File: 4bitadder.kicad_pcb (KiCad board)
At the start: 2 copper layers, 100 x 110 mm, 29 parts, among them SW1 1A, SW10 MASTER_SW, SW11 VOLTS_SW, SW2 2A, SW3 4A, SW4 8A, SW5 1B, SW6 2B, SW7 4B, SW8 8B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

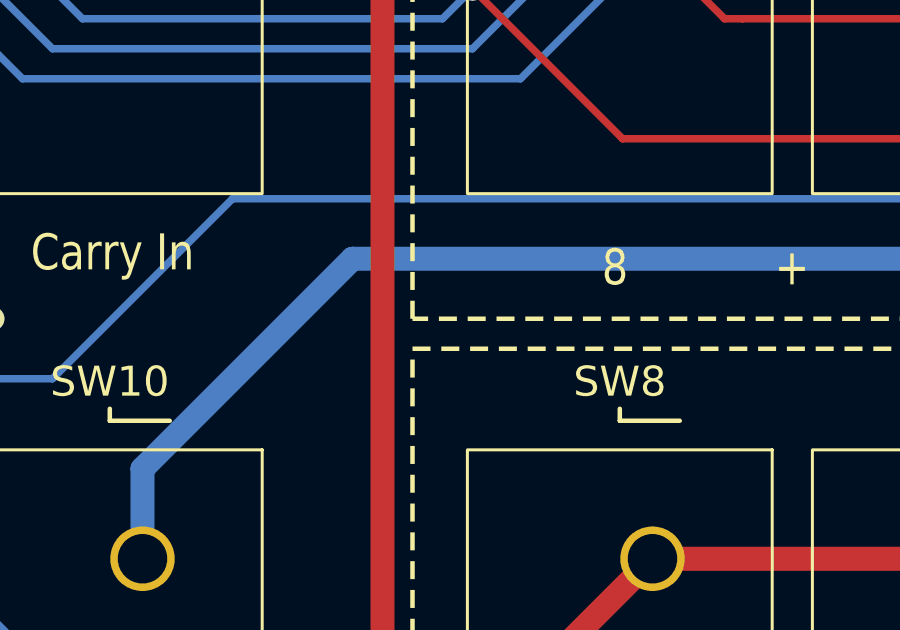
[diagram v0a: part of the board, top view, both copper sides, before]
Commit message: Change PCB Colour.
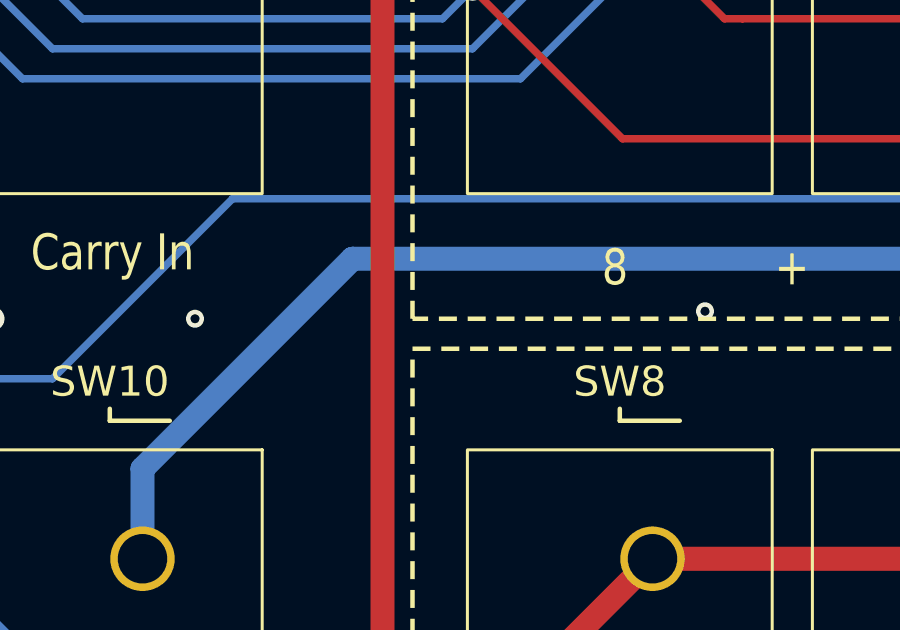
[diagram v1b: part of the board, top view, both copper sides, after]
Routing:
- net -BATT: vias 13 -> 15
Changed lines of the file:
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@@
   (via (at 85 72) (size 0.8) (drill 0.4) (layers "F.Cu" "B.Cu") (free) (net 2))
   (via (at 118 75) (size 1) (drill 0.4) (layers "F.Cu" "B.Cu") (net 2))
+  (via (at 80.75 116.75) (size 0.6) (drill 0.3) (layers "F.Cu" "B.Cu") (free) (net 2))
   (via (at 57 117) (size 0.8) (drill 0.4) (layers "F.Cu" "B.Cu") (free) (net 2))
   (via (at 73.3995 84) (size 1) (drill 0.4) (layers "F.Cu" "B.Cu") (net 2))
   (via (at 117 117) (size 0.8) (drill 0.4) (layers "F.Cu" "B.Cu") (free) (net 2))
   (via (at 70 83) (size 0.8) (drill 0.4) (layers "F.Cu" "B.Cu") (free) (net 2))
+  (via (at 63.75 117) (size 0.6) (drill 0.3) (layers "F.Cu" "B.Cu") (free) (net 2))
   (via (at 76 91) (size 0.8) (drill 0.4) (layers "F.Cu" "B.Cu") (free) (net 2))
   (segment (start 59 75) (end 58 75) (width 0.8) (layer "B.Cu") (net 2))

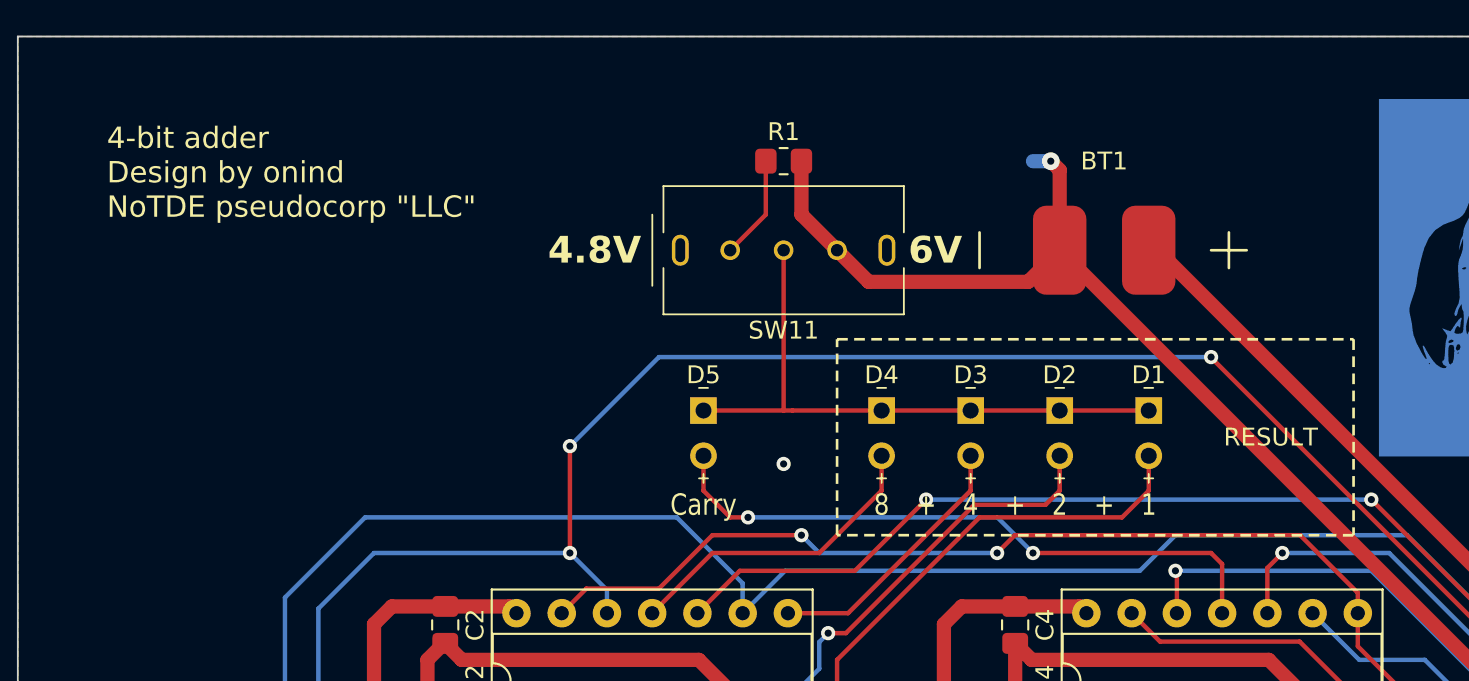
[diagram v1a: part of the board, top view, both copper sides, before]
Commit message: Repair footprint library. idk what happened there.
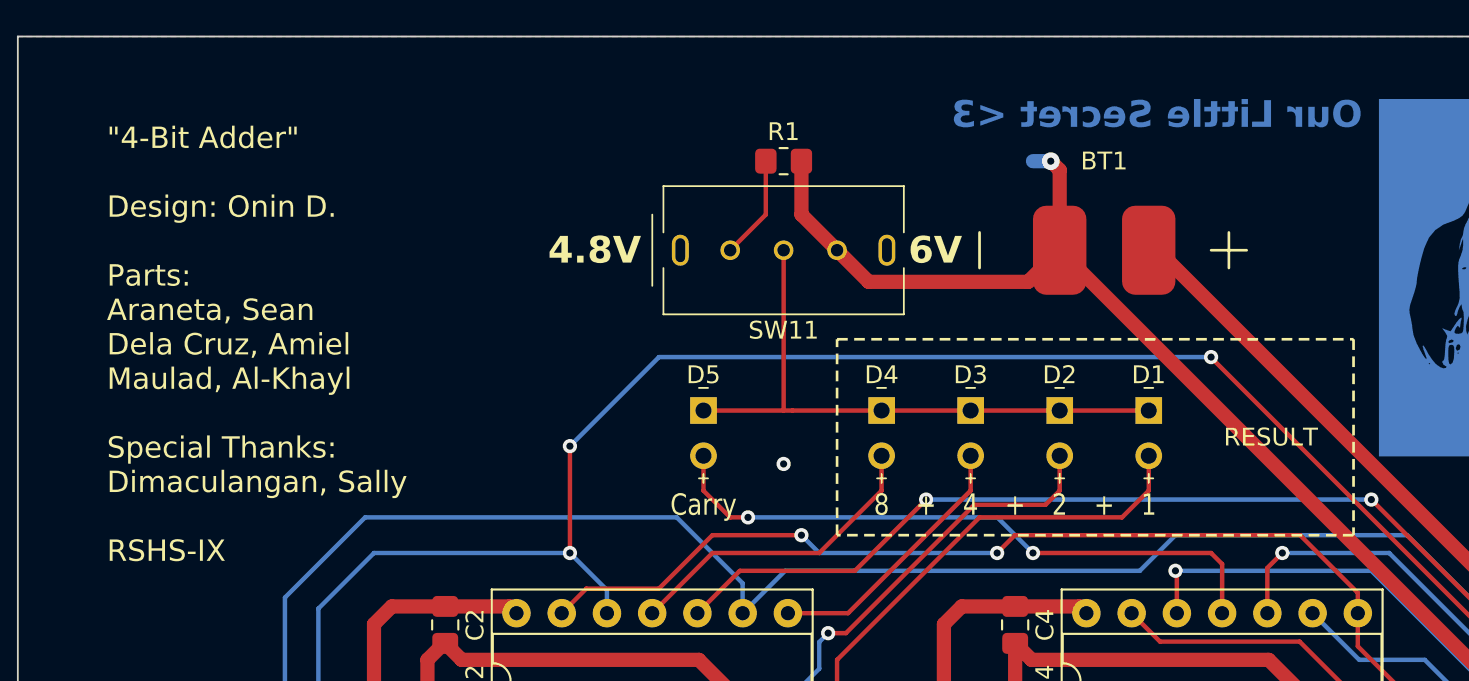
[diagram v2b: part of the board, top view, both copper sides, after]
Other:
- board text added: "Our Little Secret <3"
- board text added: "{dblquote}4-Bit Adder{dblquote} Design: Onin D. Parts: Araneta, Sean Dela Cruz, Amiel Maulad, Al-Khayl Special Thanks: Dimaculangan, Sally RSHS-IX"
- board text removed: "4-bit adder Design by onind NoTDE pseudocorp {dblquote}LLC{dblquote}"
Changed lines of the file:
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@@
   (gr_rect (start 36 34) (end 136 144)
     (stroke (width 0.1) (type default)) (fill none) (layer "Edge.Cuts"))
+  (gr_text "Our Little Secret <3" (at 111.5 37.5) (layer "B.Cu" knockout)
+    (effects (font (size 1.5 1.5) (thickness 0.3) bold) (justify left top mirror))
+  )
   (gr_text "JLCJLCJLCJLC" (at 41 42) (layer "B.SilkS")
     (effects (font (size 1 1) (thickness 0.15)) (justify right bottom mirror))
@@
     (effects (font (size 1 1) (thickness 0.15)) (justify right bottom mirror))
   )
-  (gr_text "4-bit adder\nDesign by onind\nNoTDE pseudocorp {dblquote}LLC{dblquote}" (at 41 39) (layer "F.SilkS")
+  (gr_text "{dblquote}4-Bit Adder{dblquote}\n\nDesign: Onin D.\n\nParts:\nAraneta, Sean\nDela Cruz, Amiel\nMaulad, Al-Khayl\n\nSpecial Thanks:\nDimaculangan, Sally\n\nRSHS-IX" (at 41 39) (layer "F.SilkS")
     (effects (font (size 1.2 1.2) (thickness 0.15)) (justify left top))
   )

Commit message: Finalise credits.
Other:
- board text added: "{dblquote}4-Bit Adder{dblquote} Design: Onin D. Components: Araneta, Sean Dela Cruz, Amiel Maulad, Al-Khayl Special Thanks: Dimaculangan, Sally RSHS-IX"
- board text removed: "{dblquote}4-Bit Adder{dblquote} Design: Onin D. Parts: Araneta, Sean Dela Cruz, Amiel Maulad, Al-Khayl Special Thanks: Dimaculangan, Sally RSHS-IX"
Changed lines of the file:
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@@
     (effects (font (size 1 1) (thickness 0.15)) (justify right bottom mirror))
   )
-  (gr_text "{dblquote}4-Bit Adder{dblquote}\n\nDesign: Onin D.\n\nParts:\nAraneta, Sean\nDela Cruz, Amiel\nMaulad, Al-Khayl\n\nSpecial Thanks:\nDimaculangan, Sally\n\nRSHS-IX" (at 41 39) (layer "F.SilkS")
+  (gr_text "{dblquote}4-Bit Adder{dblquote}\n\nDesign: Onin D.\n\nComponents:\nAraneta, Sean\nDela Cruz, Amiel\nMaulad, Al-Khayl\n\nSpecial Thanks:\nDimaculangan, Sally\n\nRSHS-IX" (at 41 39) (layer "F.SilkS")
     (effects (font (size 1.2 1.2) (thickness 0.15)) (justify left top))
   )

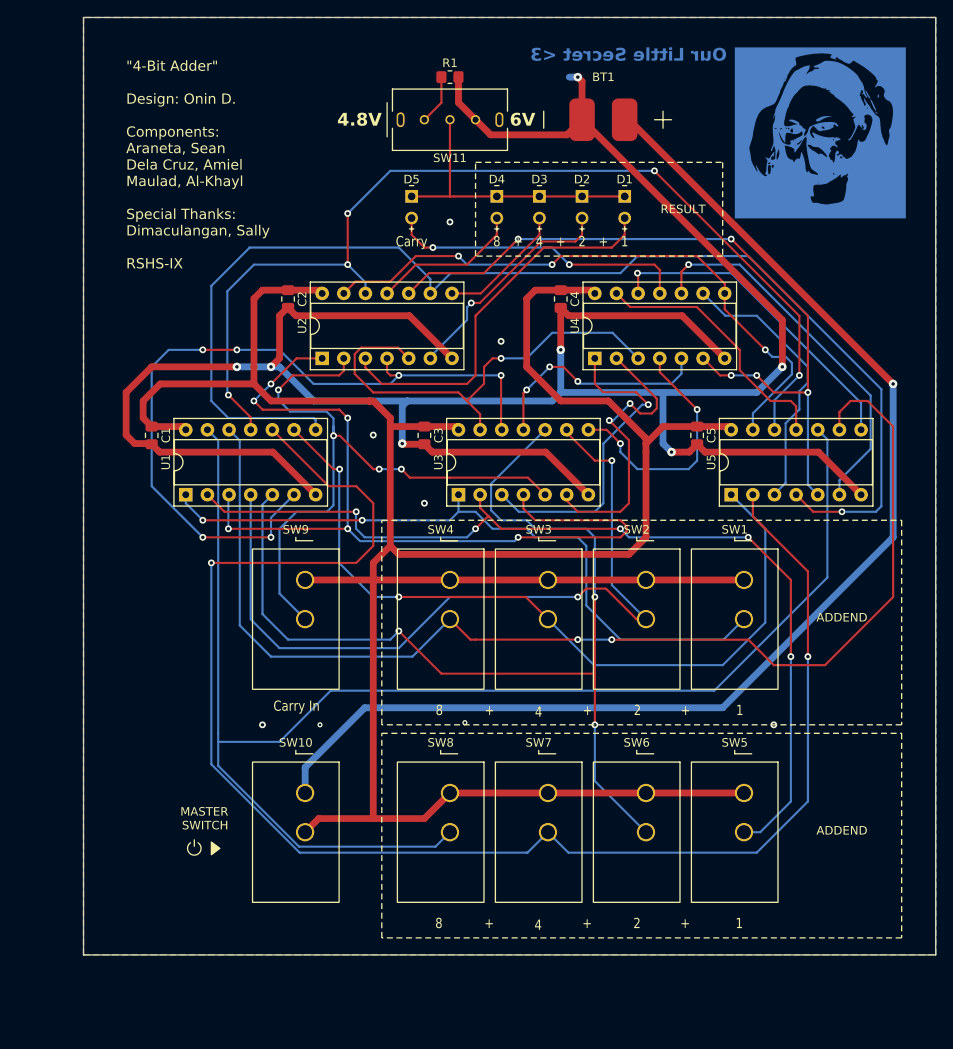
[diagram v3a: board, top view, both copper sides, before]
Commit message: Change switch design. Unroute all vias.
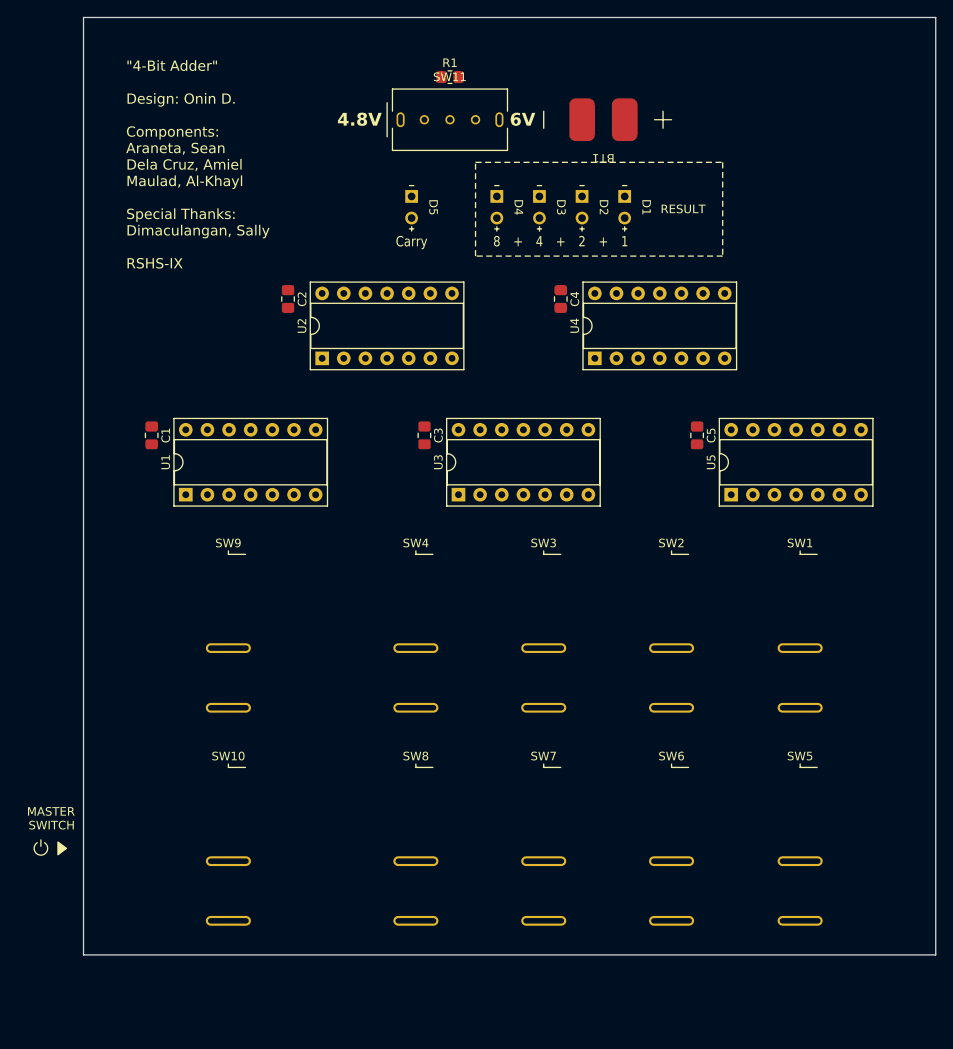
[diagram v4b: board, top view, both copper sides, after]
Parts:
- removed G***: NICA, _4bitadder:NicaPortrait
- BT1: footprint _4bitadder:PAD_Battery Terminal -> 4bitadder:PAD_Battery Terminal
- D1, D2, D3, D4, D5: footprint _4bitadder:LED_WP710A10SURDK5V -> 4bitadder:LED_WP710A10SURDK5V
- SW1, SW10, SW2, SW3, SW4, SW5, SW6, SW7, SW8, SW9: footprint _4bitadder:SW_GF-123-0054 -> 4bitadder:SW-R2-1A-F-1-0
- SW11: footprint _4bitadder:SW_SLW-121586-5A-D -> 4bitadder:SW_SLW-121586-5A-D
- moved SW10 8.61 mm to (53.0, 133.0), turned to 90 degrees
- moved SW9 8.61 mm to (53.0, 108.0), turned to 90 degrees
- moved SW1 8.40 mm to (120.1, 108.0), turned to 90 degrees
- moved SW5 8.40 mm to (120.1, 133.0), turned to 90 degrees
- moved SW2 5.32 mm to (105.0, 108.0), turned to 90 degrees
- moved SW6 5.32 mm to (105.0, 133.0), turned to 90 degrees
- moved SW4 4.48 mm to (75.0, 108.0), turned to 90 degrees
- moved SW8 4.48 mm to (75.0, 133.0), turned to 90 degrees
- moved SW3 3.45 mm to (90.0, 108.0), turned to 90 degrees
- moved SW7 3.45 mm to (90.0, 133.0), turned to 90 degrees
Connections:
- SW10 pad 1: Net-(BT1-+) -> +BATT
- SW10 pad 2: +BATT -> Net-(BT1-+)
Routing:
- net +BATT: track 306.4 -> 0.00 mm
- net -BATT: track 299.6 -> 0.00 mm, vias 15 -> 0
- net Net-(SW7-B): track 181.3 -> 0.00 mm, vias 2 -> 0
- net Net-(SW8-B): track 169.1 -> 0.00 mm
- net Net-(BT1-+): track 145.5 -> 0.00 mm, vias 1 -> 0
- net Net-(U1C-3Y): track 144.6 -> 0.00 mm, vias 1 -> 0
- net Net-(SW4-B): track 139.2 -> 0.00 mm, vias 2 -> 0
- net Net-(SW6-B): track 119.9 -> 0.00 mm, vias 3 -> 0
- net Net-(U1D-4Y): track 119.8 -> 0.00 mm, vias 5 -> 0
- net Net-(SW5-B): track 111.8 -> 0.00 mm, vias 5 -> 0
- net Net-(U1A-1Y): track 101.9 -> 0.00 mm, vias 6 -> 0
- net Net-(SW2-B): track 94.0 -> 0.00 mm, vias 2 -> 0
- net Net-(SW3-B): track 92.0 -> 0.00 mm, vias 2 -> 0
- net Net-(U1B-2Y): track 90.1 -> 0.00 mm, vias 6 -> 0
- net Net-(U2C-3B): track 88.6 -> 0.00 mm, vias 5 -> 0
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- removed copper zone on B.Cu, net -BATT
- removed copper zone on F.Cu, net -BATT
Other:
- board text removed: "ADDEND"
- board text removed: "Carry In"
- board text removed: "Our Little Secret <3"

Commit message: Add docs. Revise PCB.
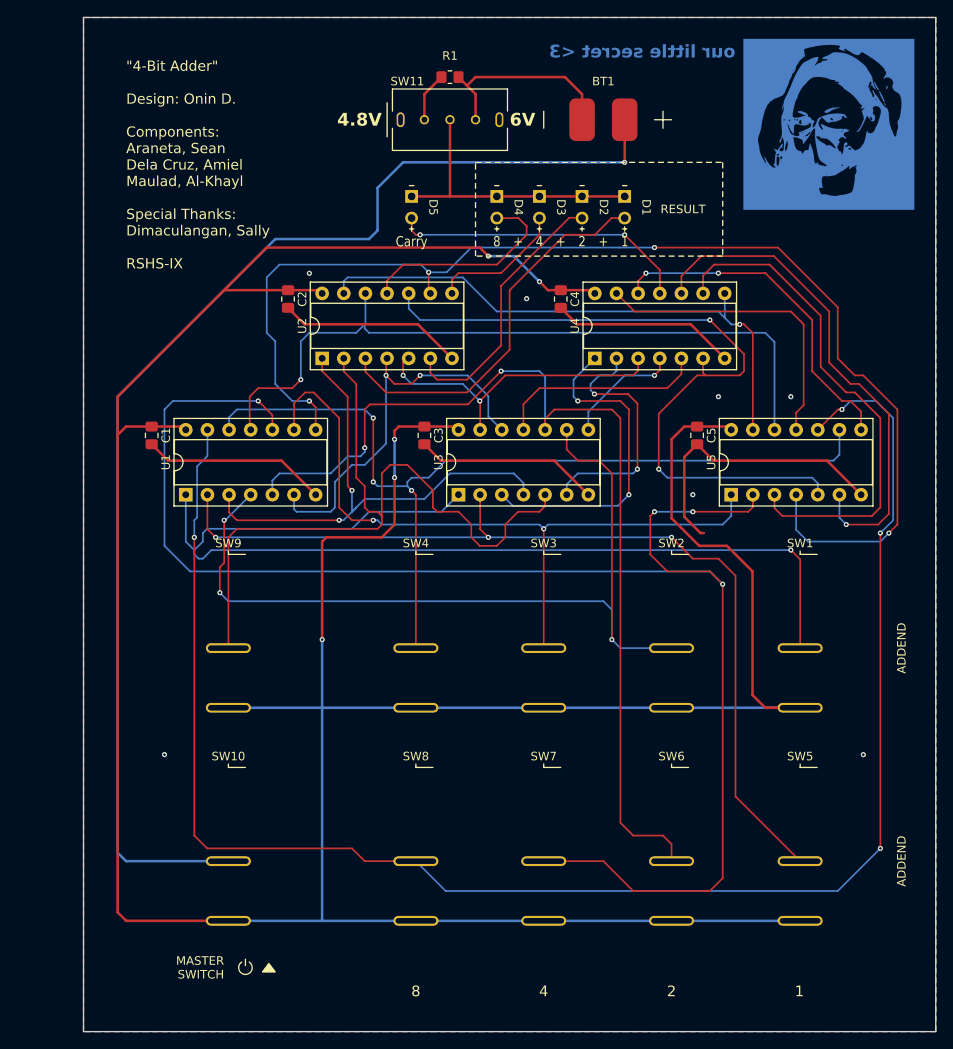
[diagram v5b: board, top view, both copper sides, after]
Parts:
- added G***: NICA, 4bitadder:NicaPortrait, B.Cu at (123.5, 46.5)
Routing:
- net +BATT: track 0.00 -> 416.3 mm, vias 0 -> 5
- net Net-(SW8-B): track 0.00 -> 195.7 mm, vias 0 -> 4
- net Net-(SW7-B): track 0.00 -> 184.8 mm, vias 0 -> 4
- net Net-(BT1-+): track 0.00 -> 145.7 mm, vias 0 -> 1
- net -BATT: track 0.00 -> 144.3 mm, vias 0 -> 7
- net Net-(U1C-3Y): track 0.00 -> 142.5 mm, vias 0 -> 4
- net Net-(SW1-B): track 0.00 -> 124.3 mm, vias 0 -> 1
- net Net-(SW6-B): track 0.00 -> 115.9 mm, vias 0 -> 2
- net Net-(SW5-B): track 0.00 -> 110.3 mm, vias 0 -> 3
- net Net-(SW4-B): track 0.00 -> 105.7 mm, vias 0 -> 3
- net Net-(SW2-B): track 0.00 -> 99.1 mm, vias 0 -> 3
- net Net-(SW9-B): track 0.00 -> 88.3 mm
- net Net-(U1D-4Y): track 0.00 -> 86.9 mm, vias 0 -> 1
- net Net-(U2C-3B): track 0.00 -> 86.7 mm, vias 0 -> 2
- net Net-(SW3-B): track 0.00 -> 84.8 mm, vias 0 -> 2
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- added copper zone on B.Cu, net -BATT
- added copper zone on F.Cu, net -BATT
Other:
- board size 100 x 110 mm -> 100 x 119 mm
- board text added: "ADDEND"
- board text added: "our little secret <3"
